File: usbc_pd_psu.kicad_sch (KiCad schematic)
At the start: 53 parts, among them J1 USB-C 5 A, J2 OUTPUT, J3 PROG, J4 OLED 0.96in I2C, Q1 AON6324, Q2 AON6324, Q3 AON6324, Q4 AON6324, Q5 TIP127, SW1 EC11, SW2 OUTPUT, SW3 SELECT, SW4 BACK, U1 CH224K, U2 IR2104, U3 IR2104, U4 LM358, U5 LP2950-5.0, U6 CH32V203C8T6, U7 LM2903

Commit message: Split the design into a hierarchy
Three sheets: a title page carrying the specification and the sheet index, the
power path, and the control and user interface.

The single sheet had become unreadable and there was no space left for the
gate-drive rail the design still needs.  Splitting it also means the power
stage and the control side can be worked on without one disturbing the other.

Nets that cross a sheet boundary use global labels, which is the only
construct KiCad merges across sheet files.  Everything local stays a real
pin-to-pin wire.
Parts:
- removed C1: 100u/35V, Capacitor_SMD:CP_Elec_6.3x7.7, symbol Device:C_Polarized
- removed C2: 22u/35V, Capacitor_SMD:C_0805_2012Metric, symbol Device:C
- removed C3, C4, C8, C9: 100nF, Capacitor_SMD:C_0805_2012Metric, symbol Device:C
- removed C5: 220u/25V, Capacitor_SMD:CP_Elec_6.3x7.7, symbol Device:C_Polarized
- removed C6, C7: 10u, Capacitor_SMD:C_0805_2012Metric, symbol Device:C
- removed D1: SMBJ24A, Diode_SMD:D_SMA, symbol Device:D_TVS
- removed D2, D3: 1N4148W, Diode_SMD:D_SOD-123, symbol Diode:1N4148W
- removed D4: red, LED_SMD:LED_0805_2012Metric, symbol Device:LED
- removed D5: amber, LED_SMD:LED_0805_2012Metric, symbol Device:LED
- removed D6: green, LED_SMD:LED_0805_2012Metric, symbol Device:LED
- removed F1: 3 A hold, Fuse:Fuse_1206_3216Metric, symbol Device:Polyfuse
- removed J1: USB-C 5 A, Connector_USB:USB_C_Receptacle_XKB_U262-16XN-4BVC11, symbol Connector:USB_C_Receptacle_PowerOnly_6P
- removed J2: OUTPUT, Connector_PinSocket_2.54mm:PinSocket_1x02_P2.54mm_Vertical, symbol Connector_Generic:Conn_01x02
- removed J3: PROG, Connector_PinHeader_2.54mm:PinHeader_1x04_P2.54mm_Vertical, symbol Connector_Generic:Conn_01x04
- removed J4: OLED 0.96in I2C, Connector_PinHeader_2.54mm:PinHeader_1x04_P2.54mm_Vertical, symbol Connector_Generic:Conn_01x04
- removed L1: 22u 5A, Inductor_SMD:L_12x12mm_H8mm, symbol Device:L
- removed Q1, Q2, Q3, Q4: AON6324, Package_TO_SOT_SMD:TO-263-2, symbol Transistor_FET:Q_NMOS_GDS
- removed Q5: TIP127, Package_TO_SOT_THT:TO-220-3_Vertical, symbol Transistor_BJT:TIP127
- removed R1, R7: 100k 1%, Resistor_SMD:R_0805_2012Metric, symbol Device:R
- removed R10, R16, R9: 10k, Resistor_SMD:R_0805_2012Metric, symbol Device:R
- removed R11, R12, R13, R4: 1k, Resistor_SMD:R_0805_2012Metric, symbol Device:R
- removed R14, R2, R6, R8: 10k 1%, Resistor_SMD:R_0805_2012Metric, symbol Device:R
- removed R15: 4k7 1%, Resistor_SMD:R_0805_2012Metric, symbol Device:R
- removed R3: 0R05 2W, Resistor_SMD:R_2512_6332Metric, symbol Device:R
- removed R5: 39k 1%, Resistor_SMD:R_0805_2012Metric, symbol Device:R
- removed SW1: EC11, Rotary_Encoder:RotaryEncoder_Alps_EC11E-Switch_Vertical_H20mm, symbol Device:RotaryEncoder_Switch
- removed SW2: OUTPUT, Button_Switch_SMD:SW_SPST_B3S-1000, symbol Switch:SW_Push
- removed SW3: SELECT, Button_Switch_SMD:SW_SPST_B3S-1000, symbol Switch:SW_Push
- removed SW4: BACK, Button_Switch_SMD:SW_SPST_B3S-1000, symbol Switch:SW_Push
- removed U1: CH224K, Package_SO:SSOP-10-1EP_3.9x4.9mm_P1mm_EP2.1x3.3mm, symbol Interface_USB:CH224K
- removed U2, U3: IR2104, Package_SO:SOIC-8_3.9x4.9mm_P1.27mm, symbol Driver_FET:IR2104
- removed U4: LM358, Package_SO:SOIC-8_3.9x4.9mm_P1.27mm, symbol Amplifier_Operational:LM358
- removed U5: LP2950-5.0, Package_TO_SOT_SMD:SOT-223-3_TabPin2, symbol Regulator_Linear:LP2950-5.0_TO92
- removed U6: CH32V203C8T6, Package_QFP:LQFP-48_7x7mm_P0.5mm, symbol MCU_WCH_CH32V2:CH32V203CxTx
- removed U7: LM2903, Package_SO:SOIC-8_3.9x4.9mm_P1.27mm, symbol Comparator:LM2903
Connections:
- no-connect marks 13 -> 0
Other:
- added sheet Control and UI (control.kicad_sch)
- added sheet Power Path (power.kicad_sch)
- note added: "(c) 2026 Mohammadreza Safaeian. All rights reserved."
- note added: "0 - 36 V / 0 - 3 A adjustable bench supply from a USB-C PD source"
- note added: "0 - 36 V, 0 - 3 A"
- note added: "1 input / PD trigger"
- note added: "10 mV / 10 mA, PWM reference + 2-pole RC"
- note added: "10 user interface"
- note added: "11 programming header"
- note added: "2 +12 V gate rail"
- note added: "3 buck-boost power stage"
- note added: "4 gate drivers"
- note added: "4-switch synchronous buck-boost, 250 kHz"
- note added: "5 over-current trip"
- note added: "7 linear post-regulator"
- note added: "8 current sense"
- note added: "9 MCU"
- note added: "BLOCK DIAGRAM"
- note added: "Buck-boost"
- note added: "CH32V003F4P6"
- note added: "CH32V203C8T6"
- note added: "Change"
- note added: "Control"
- note added: "DESIGNED AND DRAWN BY"
- note added: "Embedded Systems & Hardware Engineer"
- note added: "INA181"
- note added: "Input"
- note added: "MCU"
- note added: "Modes"
- note added: "Mohammadreza Safaeian"
- note added: "OUT"
- note added: "Output"
- note added: "PD sink"
- note added: "PNP Darlington linear stage, tracking headroom"
- note added: "PNP linear"
- note added: "Post-regulator"
- note added: "Pre-regulator"
- note added: "Protection"
- note added: "REVISION HISTORY"
- note added: "Readback"
- note added: "Rev"
- note added: "SPECIFICATION"
- note added: "STM32G030C8T6"
- note added: "STM32G030C8T6 - PWM, ADC, PD contract, panel"
- note added: "STM32G030C8T6, OLED + rotary encoder + 3 keys"
- note added: "Set resolution"
- note added: "Shunt +"
- note added: "USB-C"
- note added: "USB-C PD BENCH POWER SUPPLY"
- note added: "USB-C PD sink, 5 / 9 / 12 / 15 / 20 V contracts"
- note added: "constant voltage, constant current, battery emulation"
- note added: "first bench build; NPN Darlington follower"
- note added: "front panel added; the '003 runs out of pins"
- note added: "github.com/mohammadrezasafaeian"
- note added: "hardware over-current trip"
- note added: "hardware over-current trip, latching"
- note added: "m.re.safaeian@gmail.com"
- note added: "pass device turned round to a PNP"
- note added: "post-reg"
- note added: "pre-reg"
- note added: "redrawn as a hierarchy; on-sheet 12 V rail"
- note added: "v0.3"
- note added: "v0.4"
- note added: "v0.5"
- note added: "v0.6"
- note added: "v1.1"
- note added: "voltage and current, 12-bit ADC"
- note removed: "1 - USB-C PD INPUT"
- note removed: "2 - 4-SWITCH BUCK-BOOST (MCU PWM - no switcher IC)"
- note removed: "3 - LINEAR POST-REG + CURRENT SENSE"
- note removed: "4 - +5 V LDO"
- note removed: "5 - MCU"
- note removed: "6 - PROG / UART"
- note removed: "7 - USER INTERFACE"
- note removed: "8 - HARDWARE OVER-CURRENT TRIP"

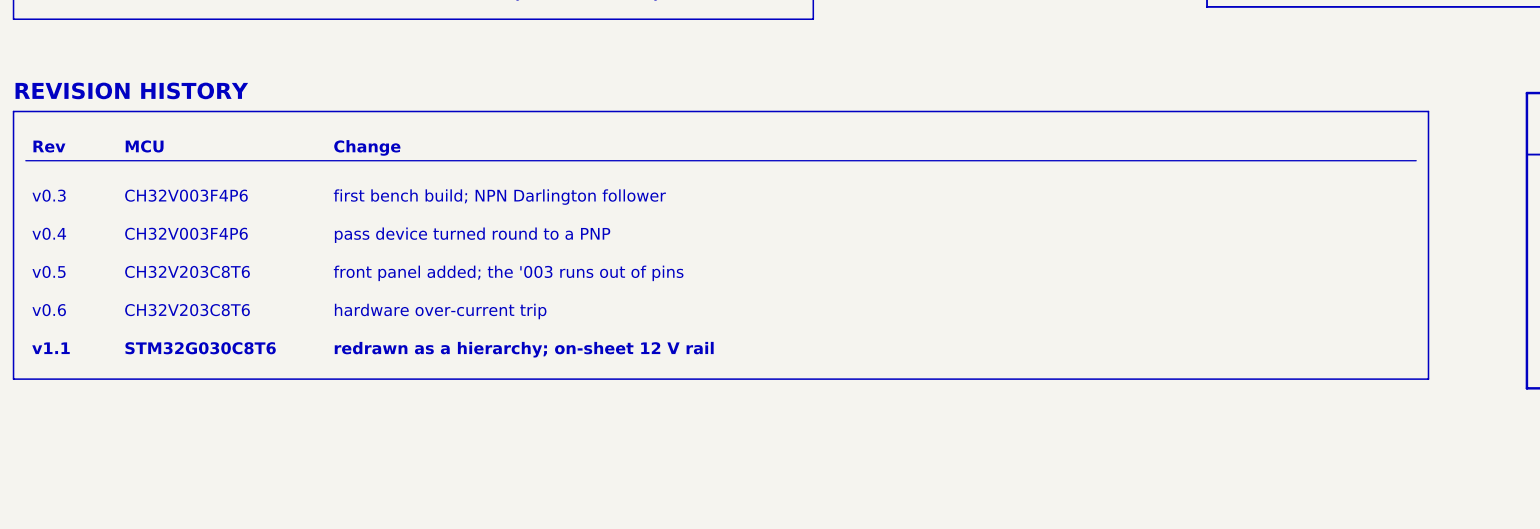
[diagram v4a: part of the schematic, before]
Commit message: v1.2: 0-36 V range, and analogue nets onto real ADC pins
Two changes, one of them serious.

The serious one: ADC_VBUS, ADC_VPRE, ADC_VOUT and ISNS_OUT were on PD2, PD3,
PC6 and PC7.  None of those four pins has an ADC channel on this part, so not
one of the four measurements could ever have been taken.  They move to PA0,
PA1, PA4 and PA5 - ADC_IN0, 1, 4 and 5 - and the timer outputs shuffle to
suit.

The range change: the feedback divider goes from 39k/10k to 150k/10k, which
puts 36 V at the top of the range instead of 20 V, and the divider ratio
becomes exactly 16:1 so the reference maths stays integer.  The pre-regulator
bulk capacitor and the output capacitor go to 63 V parts to match, and the
monitor dividers are rescaled the same way.
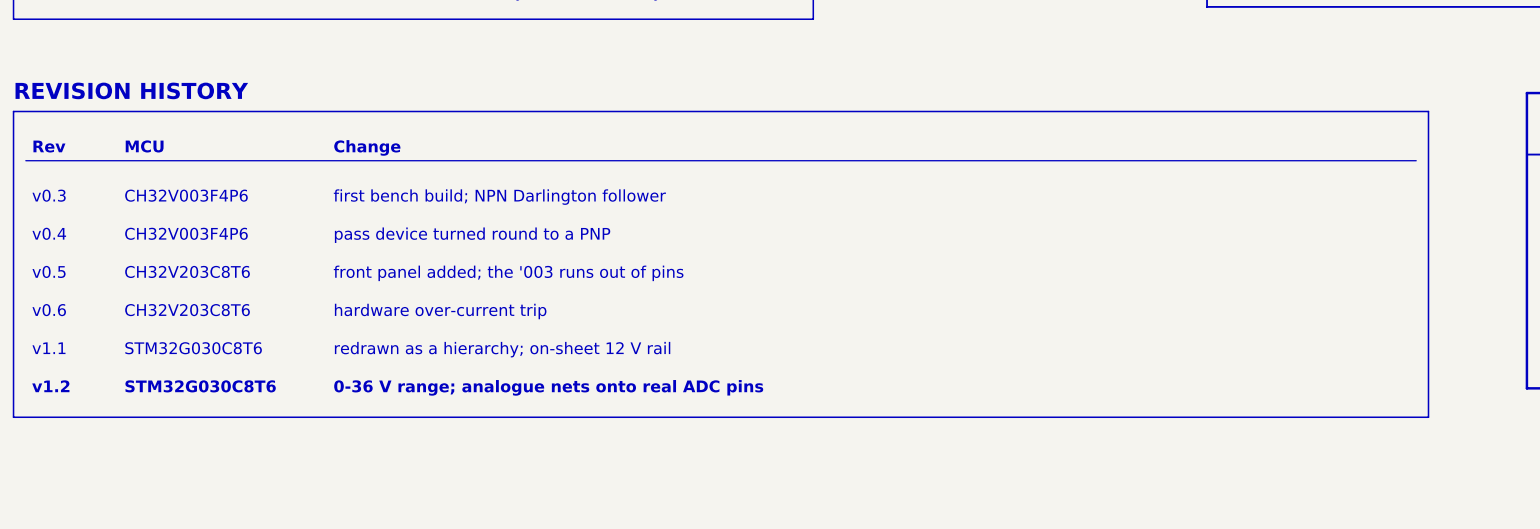
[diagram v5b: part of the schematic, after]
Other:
- note added: "0-36 V range; analogue nets onto real ADC pins"
- note added: "v1.2"
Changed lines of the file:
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@@
 (title_block
 (title "USB-C PD Bench PSU  -  4-Switch Buck-Boost + PNP Linear Post-Regulator")
-(date "2026-04-15")
-(rev "v1.1")
+(date "2026-04-25")
+(rev "v1.2")
 (company "Mohammadreza Safaeian  -  personal project")
 (comment 1 "Title page  -  specification, block diagram, sheet index")
@@
 (text "CH32V203C8T6" (at 38 155.59999999999997 0) (effects (font (size 1.9 1.9)  ) (justify left)))
 (text "hardware over-current trip" (at 72 155.59999999999997 0) (effects (font (size 1.9 1.9)  ) (justify left)))
-(text "v1.1" (at 23 161.79999999999995 0) (effects (font (size 1.9 1.9) (bold yes) (color 32 96 176 1)) (justify left)))
-(text "STM32G030C8T6" (at 38 161.79999999999995 0) (effects (font (size 1.9 1.9) (bold yes) ) (justify left)))
-(text "redrawn as a hierarchy; on-sheet 12 V rail" (at 72 161.79999999999995 0) (effects (font (size 1.9 1.9) (bold yes) ) (justify left)))
-(rectangle (start 20 123) (end 250 166.49999999999994) (stroke (width 0.25) (type solid) (color 120 120 120 1)) (fill (type none)))
+(text "v1.1" (at 23 161.79999999999995 0) (effects (font (size 1.9 1.9)  ) (justify left)))
+(text "STM32G030C8T6" (at 38 161.79999999999995 0) (effects (font (size 1.9 1.9)  ) (justify left)))
+(text "redrawn as a hierarchy; on-sheet 12 V rail" (at 72 161.79999999999995 0) (effects (font (size 1.9 1.9)  ) (justify left)))
+(text "v1.2" (at 23 167.99999999999994 0) (effects (font (size 1.9 1.9) (bold yes) (color 32 96 176 1)) (justify left)))
+(text "STM32G030C8T6" (at 38 167.99999999999994 0) (effects (font (size 1.9 1.9) (bold yes) ) (justify left)))
+(text "0-36 V range; analogue nets onto real ADC pins" (at 72 167.99999999999994 0) (effects (font (size 1.9 1.9) (bold yes) ) (justify left)))
+(rectangle (start 20 123) (end 250 172.69999999999993) (stroke (width 0.25) (type solid) (color 120 120 120 1)) (fill (type none)))
 (sheet (at 20.32 256.54) (size 120 30)
 (exclude_from_sim no) (in_bom yes) (on_board yes) (dnp no)
@@
 (property "Sheetname" "Power Path" (at 20.32 255.54000000000002 0) (effects (font (size 2.0 2.0) (bold yes)) (justify left bottom)))
 (property "Sheetfile" "power.kicad_sch" (at 20.32 287.94 0) (effects (font (size 1.3 1.3)) (justify left top)))
-(instances (project "usbc_pd_psu" (path "/faa90237-9839-4d25-a155-f6b1445aeede" (page "2"))))
+(instances (project "usbc_pd_psu" (path "/cfbe660d-66b4-4905-b833-d8bc0ffe4180" (page "2"))))
 )
 (sheet (at 152.4 256.54) (size 120 30)
@@
 (property "Sheetname" "Control and UI" (at 152.4 255.54000000000002 0) (effects (font (size 2.0 2.0) (bold yes)) (justify left bottom)))
 (property "Sheetfile" "control.kicad_sch" (at 152.4 287.94 0) (effects (font (size 1.3 1.3)) (justify left top)))
-(instances (project "usbc_pd_psu" (path "/faa90237-9839-4d25-a155-f6b1445aeede" (page "3"))))
+(instances (project "usbc_pd_psu" (path "/cfbe660d-66b4-4905-b833-d8bc0ffe4180" (page "3"))))
 )
 (text "1  input / PD trigger" (at 25 266 0) (effects (font (size 1.7 1.7)  ) (justify left)))
@@
 (sheet_instances
 (path "/" (page "1"))
-(path "/024eb734-39e4-4276-ba03-79435cb44626" (page "2"))
-(path "/82821ce0-b9b4-4762-a663-8899379f440f" (page "3"))
+(path "/c668c62b-0919-4e24-8058-92970f560e50" (page "2"))
+(path "/339009a7-3f79-484c-b072-0a11d6a1ad9e" (page "3"))
 )
 )

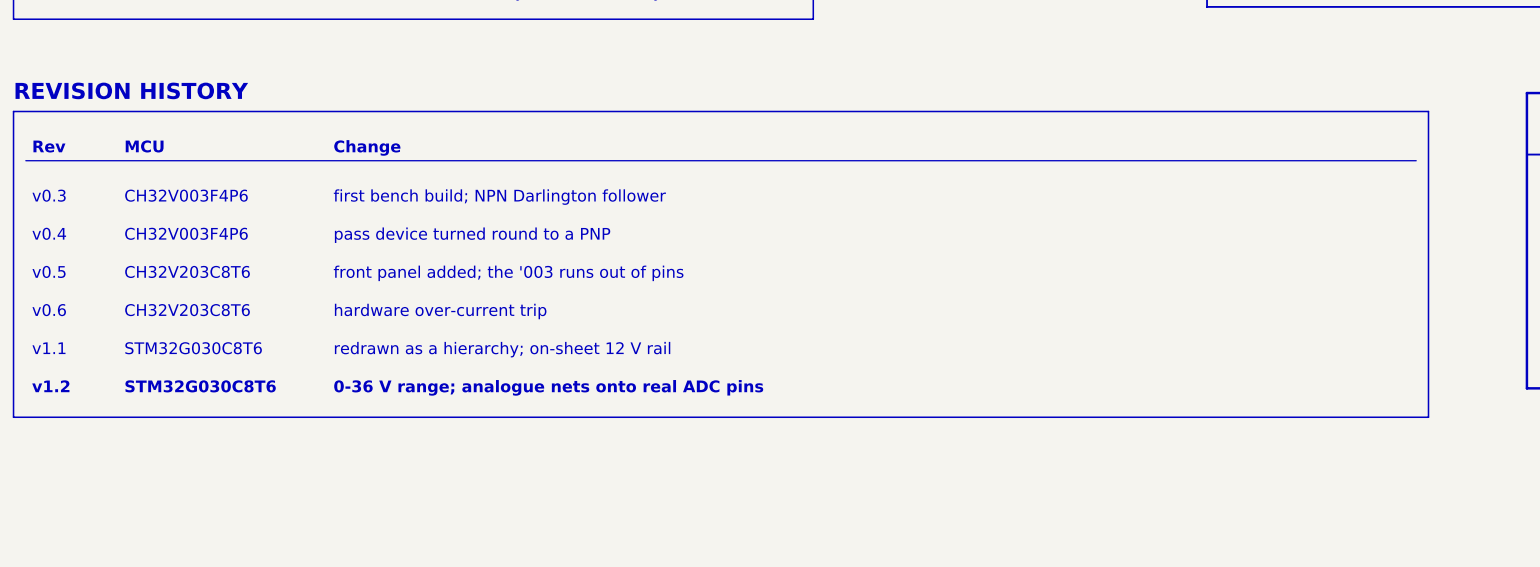
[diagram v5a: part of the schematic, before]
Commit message: v1.3: close the feedback loop, tie the driver returns, rescale the sense chain
Three faults, each of which on its own would have stopped the board working.
All three came out of reading the exported netlist rather than the schematic.

The feedback loop was never closed.  The output divider tap and the error
amplifier's inverting input were two separate nets: the divider went only to an
MCU analogue input, and the amplifier input saw only its compensation
capacitor.  With no DC path around it the amplifier is a bare integrator - its
input floats on bias current and its output ramps to a rail - so the pass
device would have sat hard on or hard off.  The output would not have
regulated; it would have latched.  Both now carry one name and are one node,
which gives V_OUT = 16 x V_REF, exactly what set_ref_dac() already assumes.

The high-side driver returns were open.  Each IRS2104's VS pin sat on a net of
its own instead of on the switch node it references.  VS is what the bootstrap
capacitor and the high-side output float on, so with it open the capacitor
cannot refresh and neither high-side FET switches at all.  Both now tie to the
power switch node.

The current sense saturated at 1.32 A.  0.05 ohm into a gain of 50 is 2.5 V/A,
which reaches the 3.3 V ADC ceiling well below the 3 A the shunt and the pass
device are rated for.  Above that the reading sticks, so the current limit, the
constant-current indicator and the adaptive headroom all stop responding while
the analogue loop carries on delivering current.  0.01 ohm into a gain of 100
gives 1 V/A: full scale 3.3 A, and a fifth of the dissipation in the shunt.

That last change also makes the over-current trip reachable.  At 2.5 V/A a
3.2 A threshold needed 8 V of reference, which the 5 V rail cannot produce, so
the divider had been set to whatever fitted and tripped at 0.64 A.  At 1 V/A
the same threshold needs 3.2 V, and 22k over 39k puts it there.

ERC is clean apart from the library-symbol mismatches that come f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
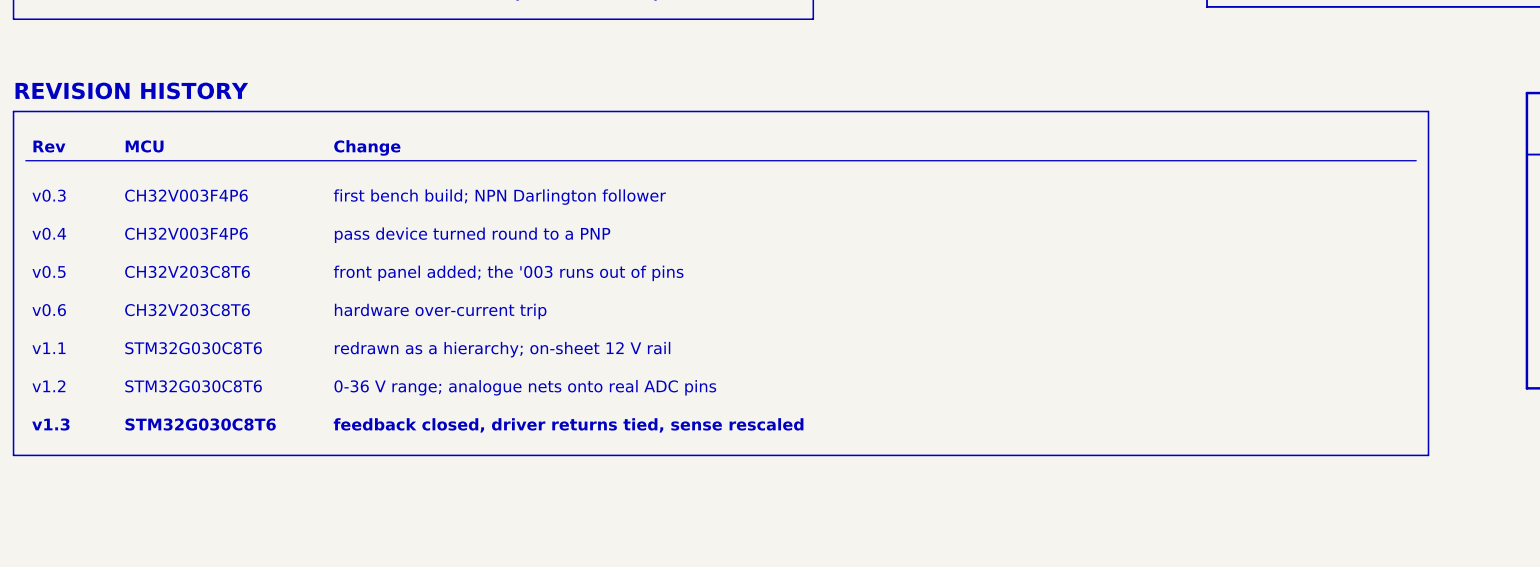
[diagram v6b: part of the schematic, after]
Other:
- note added: "feedback closed, driver returns tied, sense rescaled"
- note added: "v1.3"
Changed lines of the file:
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@@
 (title_block
 (title "USB-C PD Bench PSU  -  4-Switch Buck-Boost + PNP Linear Post-Regulator")
-(date "2026-04-25")
-(rev "v1.2")
+(date "2026-05-25")
+(rev "v1.3")
 (company "Mohammadreza Safaeian  -  personal project")
 (comment 1 "Title page  -  specification, block diagram, sheet index")
@@
 (text "STM32G030C8T6" (at 38 161.79999999999995 0) (effects (font (size 1.9 1.9)  ) (justify left)))
 (text "redrawn as a hierarchy; on-sheet 12 V rail" (at 72 161.79999999999995 0) (effects (font (size 1.9 1.9)  ) (justify left)))
-(text "v1.2" (at 23 167.99999999999994 0) (effects (font (size 1.9 1.9) (bold yes) (color 32 96 176 1)) (justify left)))
-(text "STM32G030C8T6" (at 38 167.99999999999994 0) (effects (font (size 1.9 1.9) (bold yes) ) (justify left)))
-(text "0-36 V range; analogue nets onto real ADC pins" (at 72 167.99999999999994 0) (effects (font (size 1.9 1.9) (bold yes) ) (justify left)))
-(rectangle (start 20 123) (end 250 172.69999999999993) (stroke (width 0.25) (type solid) (color 120 120 120 1)) (fill (type none)))
+(text "v1.2" (at 23 167.99999999999994 0) (effects (font (size 1.9 1.9)  ) (justify left)))
+(text "STM32G030C8T6" (at 38 167.99999999999994 0) (effects (font (size 1.9 1.9)  ) (justify left)))
+(text "0-36 V range; analogue nets onto real ADC pins" (at 72 167.99999999999994 0) (effects (font (size 1.9 1.9)  ) (justify left)))
+(text "v1.3" (at 23 174.19999999999993 0) (effects (font (size 1.9 1.9) (bold yes) (color 32 96 176 1)) (justify left)))
+(text "STM32G030C8T6" (at 38 174.19999999999993 0) (effects (font (size 1.9 1.9) (bold yes) ) (justify left)))
+(text "feedback closed, driver returns tied, sense rescaled" (at 72 174.19999999999993 0) (effects (font (size 1.9 1.9) (bold yes) ) (justify left)))
+(rectangle (start 20 123) (end 250 178.89999999999992) (stroke (width 0.25) (type solid) (color 120 120 120 1)) (fill (type none)))
 (sheet (at 20.32 256.54) (size 120 30)
 (exclude_from_sim no) (in_bom yes) (on_board yes) (dnp no)
@@
 (property "Sheetname" "Power Path" (at 20.32 255.54000000000002 0) (effects (font (size 2.0 2.0) (bold yes)) (justify left bottom)))
 (property "Sheetfile" "power.kicad_sch" (at 20.32 287.94 0) (effects (font (size 1.3 1.3)) (justify left top)))
-(instances (project "usbc_pd_psu" (path "/cfbe660d-66b4-4905-b833-d8bc0ffe4180" (page "2"))))
+(instances (project "usbc_pd_psu" (path "/ad0ff90b-e819-417c-9408-5310bafd8a03" (page "2"))))
 )
 (sheet (at 152.4 256.54) (size 120 30)
@@
 (property "Sheetname" "Control and UI" (at 152.4 255.54000000000002 0) (effects (font (size 2.0 2.0) (bold yes)) (justify left bottom)))
 (property "Sheetfile" "control.kicad_sch" (at 152.4 287.94 0) (effects (font (size 1.3 1.3)) (justify left top)))
-(instances (project "usbc_pd_psu" (path "/cfbe660d-66b4-4905-b833-d8bc0ffe4180" (page "3"))))
+(instances (project "usbc_pd_psu" (path "/ad0ff90b-e819-417c-9408-5310bafd8a03" (page "3"))))
 )
 (text "1  input / PD trigger" (at 25 266 0) (effects (font (size 1.7 1.7)  ) (justify left)))
@@
 (sheet_instances
 (path "/" (page "1"))
-(path "/c668c62b-0919-4e24-8058-92970f560e50" (page "2"))
-(path "/339009a7-3f79-484c-b072-0a11d6a1ad9e" (page "3"))
+(path "/aadf946a-5c87-4627-9e34-a652e43829c2" (page "2"))
+(path "/4cff5293-c6eb-4b1b-848c-23bdcb519bb1" (page "3"))
 )
 )
